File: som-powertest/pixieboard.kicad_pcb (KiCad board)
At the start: 8 copper layers, 50 x 50 mm, 138 parts, among them J1 Conn_02x20_Counter_Clockwise, J2 Conn_02x20_Counter_Clockwise, J3 Conn_02x20_Counter_Clockwise, J4 Conn_02x20_Counter_Clockwise, J5 Conn_02x20_Counter_Clockwise, J6 Conn_02x20_Counter_Clockwise, J7 Conn_02x20_Counter_Clockwise, U10 RS3236-ADJ8YF5, U5 SIC402, U6 RS3236-ADJ8YF5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

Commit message: Migrate evey power wire off layers in3-in6
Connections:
- J1 pad 10: Net-(J1-Pin_10) -> unconnected-(J1-Pin_10-Pad10)
- J1 pad 12: Net-(J1-Pin_12) -> unconnected-(J1-Pin_12-Pad12)
- J1 pad 13: Net-(J1-Pin_13) -> unconnected-(J1-Pin_13-Pad13)
- J1 pad 15: Net-(J1-Pin_15) -> unconnected-(J1-Pin_15-Pad15)
- J1 pad 16: Net-(J1-Pin_16) -> unconnected-(J1-Pin_16-Pad16)
- J1 pad 18: Net-(J1-Pin_18) -> unconnected-(J1-Pin_18-Pad18)
- J1 pad 19: Net-(J1-Pin_19) -> unconnected-(J1-Pin_19-Pad19)
- J1 pad 22: Net-(J1-Pin_19) -> unconnected-(J1-Pin_22-Pad22)
- J1 pad 23: Net-(J1-Pin_18) -> unconnected-(J1-Pin_23-Pad23)
- J1 pad 25: Net-(J1-Pin_16) -> unconnected-(J1-Pin_25-Pad25)
- J1 pad 26: Net-(J1-Pin_15) -> unconnected-(J1-Pin_26-Pad26)
- J1 pad 28: Net-(J1-Pin_13) -> unconnected-(J1-Pin_28-Pad28)
- J1 pad 29: Net-(J1-Pin_12) -> unconnected-(J1-Pin_29-Pad29)
- J1 pad 31: Net-(J1-Pin_10) -> unconnected-(J1-Pin_31-Pad31)
- J1 pad 32: Net-(J1-Pin_32) -> unconnected-(J1-Pin_32-Pad32)
- J1 pad 9: Net-(J1-Pin_32) -> unconnected-(J1-Pin_9-Pad9)
- J2 pad 11: Net-(J2-Pin_11) -> unconnected-(J2-Pin_11-Pad11)
- J2 pad 12: Net-(J2-Pin_12) -> unconnected-(J2-Pin_12-Pad12)
- J2 pad 14: Net-(J2-Pin_14) -> unconnected-(J2-Pin_14-Pad14)
- J2 pad 15: Net-(J2-Pin_15) -> unconnected-(J2-Pin_15-Pad15)
- J2 pad 17: Net-(J2-Pin_17) -> unconnected-(J2-Pin_17-Pad17)
- J2 pad 18: Net-(J2-Pin_18) -> unconnected-(J2-Pin_18-Pad18)
- J2 pad 2: Net-(J2-Pin_2) -> unconnected-(J2-Pin_2-Pad2)
- J2 pad 23: Net-(J2-Pin_18) -> unconnected-(J2-Pin_23-Pad23)
- J2 pad 24: Net-(J2-Pin_17) -> unconnected-(J2-Pin_24-Pad24)
- J2 pad 26: Net-(J2-Pin_15) -> unconnected-(J2-Pin_26-Pad26)
- J2 pad 27: Net-(J2-Pin_14) -> unconnected-(J2-Pin_27-Pad27)
- J2 pad 29: Net-(J2-Pin_12) -> unconnected-(J2-Pin_29-Pad29)
- J2 pad 3: Net-(J2-Pin_3) -> unconnected-(J2-Pin_3-Pad3)
- J2 pad 30: Net-(J2-Pin_11) -> unconnected-(J2-Pin_30-Pad30)
- J2 pad 32: Net-(J2-Pin_32) -> unconnected-(J2-Pin_32-Pad32)
- J2 pad 33: Net-(J2-Pin_33) -> unconnected-(J2-Pin_33-Pad33)
- J2 pad 35: Net-(J2-Pin_35) -> unconnected-(J2-Pin_35-Pad35)
- J2 pad 36: Net-(J2-Pin_36) -> unconnected-(J2-Pin_36-Pad36)
- J2 pad 38: Net-(J2-Pin_3) -> unconnected-(J2-Pin_38-Pad38)
- J2 pad 39: Net-(J2-Pin_2) -> unconnected-(J2-Pin_39-Pad39)
- J2 pad 5: Net-(J2-Pin_36) -> unconnected-(J2-Pin_5-Pad5)
- J2 pad 6: Net-(J2-Pin_35) -> unconnected-(J2-Pin_6-Pad6)
- J2 pad 8: Net-(J2-Pin_33) -> unconnected-(J2-Pin_8-Pad8)
- J2 pad 9: Net-(J2-Pin_32) -> unconnected-(J2-Pin_9-Pad9)
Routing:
- net /DDR_VREF: track 88.5 -> 75.2 mm, vias 8 -> 0
- net /DDR3/V_{TT}: track 70.8 -> 66.5 mm, vias 7 -> 2
- net MTGAVTT: track 38.0 -> 34.7 mm, vias 7 -> 3
- net GND: track 80.0 -> 78.3 mm
- net MTGAVCC: vias 6 -> 1
- net +1V35: vias 49 -> 15
- added copper zone on In2.Cu, net +1V35
- added copper zone on In1.Cu, net /DDR3/V_{TT}
- removed copper zone on In3.Cu, net +1V35
- removed copper zone on In5.Cu, net /DDR3/V_{TT}

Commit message: Remove layers in3-in6 from powertest pcb
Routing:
- net MTGAVTT: vias 3 -> 1
- added copper zone on In2.Cu, net GND
- removed copper zone on In5.Cu, net +1V0
- removed copper zone on In3.Cu, net GND
- removed copper zone on In5.Cu, net GND
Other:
- copper layers 8 -> 4
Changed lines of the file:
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@@
 		(4 "In1.Cu" power)
 		(6 "In2.Cu" signal)
-		(8 "In3.Cu" power)
-		(10 "In4.Cu" signal)
-		(12 "In5.Cu" power)
-		(14 "In6.Cu" signal)
 		(2 "B.Cu" power)
 		(13 "F.Paste" user)
@@
 			(layer "dielectric 1"
 				(type "prepreg")
-				(thickness 0.0994)
+				(thickness 0.1)
 				(material "FR4")
 				(epsilon_r 4.5)
@@
 			(layer "dielectric 2"
 				(type "core")
-				(thickness 0.2)
+				(thickness 0.8772)
 				(material "FR4")
 				(epsilon_r 4.5)
@@
 			(layer "dielectric 3"
 				(type "prepreg")
-				(thickness 0.1088)
-				(material "FR4")
-				(epsilon_r 4.5)
-				(loss_tangent 0.02)
-			)
-			(layer "In3.Cu"
-				(type "copper")
-				(thickness 0.0152)
-			)
-			(layer "dielectric 4"
-				(type "core")
-				(thickness 0.2)
-				(material "FR4")
-				(epsilon_r 4.5)
-				(loss_tangent 0.02)
-			)
-			(layer "In4.Cu"
-				(type "copper")
-				(thickness 0.0152)
-			)
-			(layer "dielectric 5"
-				(type "prepreg")
-				(thickness 0.1088)
-				(material "FR4")
-				(epsilon_r 4.5)
-				(loss_tangent 0.02)
-			)
-			(layer "In5.Cu"
-				(type "copper")
-				(thickness 0.0152)
-			)
-			(layer "dielectric 6"
-				(type "core")
-				(thickness 0.2)
-				(material "FR4")
-				(epsilon_r 4.5)
-				(loss_tangent 0.02)
-			)
-			(layer "In6.Cu"
-				(type "copper")
-				(thickness 0.0152)
-			)
-			(layer "dielectric 7"
-				(type "prepreg")
-				(thickness 0.0994)
+				(thickness 0.1)
 				(material "FR4")
 				(epsilon_r 4.5)
@@
 		(net 41)
 	)
-	(via
-		(at 97.5 91.5)
-		(size 0.3)
-		(drill 0.15)
-		(layers "F.Cu" "B.Cu")
-		(net 41)
-	)
-	(via
-		(at 98.5 90.500001)
-		(size 0.3)
-		(drill 0.15)
-		(layers "F.Cu" "B.Cu")
-		(net 41)
-	)
 	(segment
 		(start 100.5 90.5)
@@
 	)
 	(segment
-		(start 97.5 91.5)
-		(end 97.500001 91.5)
-		(width 0.15)
-		(layer "In6.Cu")
-		(net 41)
-	)
-	(segment
-		(start 98.5 90.500001)
-		(end 98.500001 90.500001)
-		(width 0.15)
-		(layer "In6.Cu")
-		(net 41)
-	)
-	(segment
 		(start 112.75 86.45)
 		(end 112.8975 86.5975)
@@
 		(polygon
 			(pts
-				(xy 77.1 95.4) (xy 80.7 95.4) (xy 80.7 95.8) (xy 77.1 95.8)
-			)
-		)
-	)
-	(zone
-		(net 0)
-		(net_name "")
-		(layer "B.Cu")
-		(hatch edge 0.5)
-		(connect_pads
-			(clearance 0)
-		)
-		(min_thickness 0.25)
-		(filled_areas_thickness no)
-		(keepout
-			(tracks allowed)
-			(vias allowed)
-			(pads allowed)
-			(copperpour not_allowed)
-			(footprints allowed)
-		)
-		(placement
-			(enabled no)
-			(sheetname "")
-		)
-		(fill
-			(thermal_gap 0.5)
-			(thermal_bridge_width 0.5)
-		)
-		(polygon
-			(pts
 				(xy 109.2 78.4) (xy 114.4 78.4) (xy 114.4 78.8) (xy 109.2 78.8)
 			)
@@
 		(polygon
 			(pts
-				(xy 77.1 89.4) (xy 77.1 89) (xy 80.7 89) (xy 80.7 89.4)
-			)
-		)
-	)
-	(zone
-		(net 0)
-		(net_name "")
-		(layer "B.Cu")
-		(hatch edge 0.5)
-		(connect_pads
-			(clearance 0)
-		)
-		(min_thickness 0.25)
-		(filled_areas_thickness no)
-		(keepout
-			(tracks allowed)
-			(vias allowed)
-			(pads allowed)
-			(copperpour not_allowed)
-			(footprints allowed)
-		)
-		(placement
-			(enabled no)
-			(sheetname "")
-		)
-		(fill
-			(thermal_gap 0.5)
-			(thermal_bridge_width 0.5)
-		)
-		(polygon
-			(pts
 				(xy 82.5 117.8) (xy 84.7 117.8) (xy 84.7 118.2) (xy 82.5 118.2)
 			)
@@
 		(net 3)
 		(net_name "GND")
-		(layers "B.Cu" "In1.Cu" "In3.Cu" "In5.Cu")
+		(layers "B.Cu" "In1.Cu" "In2.Cu")
 		(hatch edge 0.5)
 		(connect_pads
@@
 		(net 7)
 		(net_name "+1V0")
-		(layers "In1.Cu" "In5.Cu")
+		(layer "In1.Cu")
 		(hatch edge 0.5)
 		(priority 2)

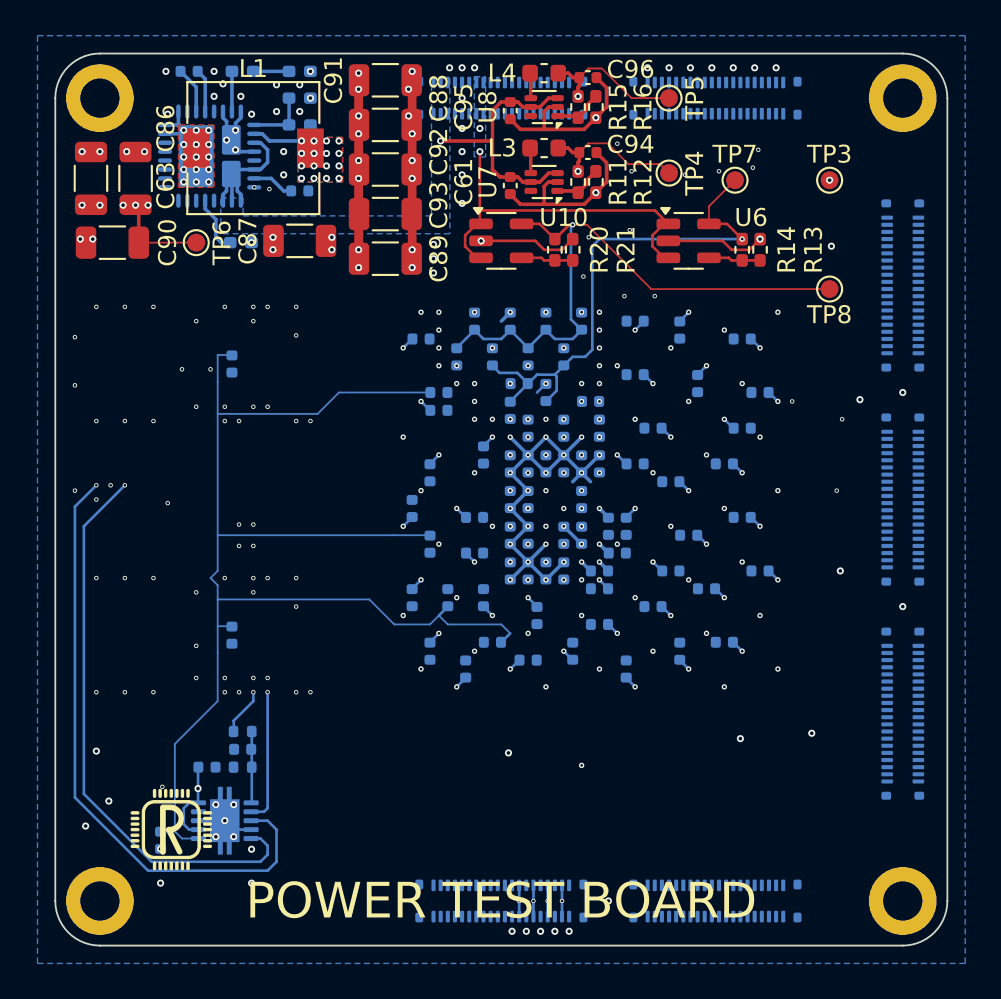
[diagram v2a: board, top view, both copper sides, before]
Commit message: Add large pads for connection to a synthetic load
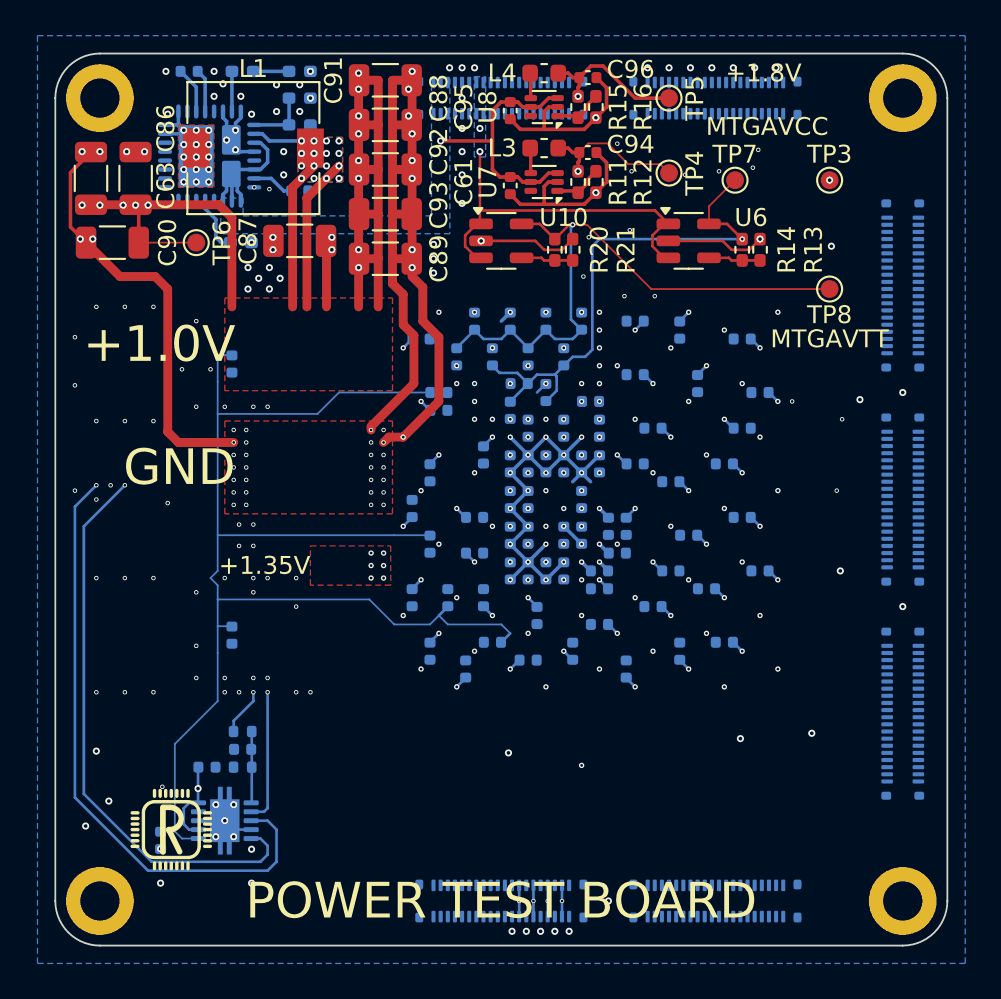
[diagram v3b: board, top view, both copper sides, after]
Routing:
- net GND: track 78.3 -> 140.5 mm, vias 248 -> 268
- net +1V0: track 19.2 -> 74.0 mm
- net +1V35: vias 15 -> 21
- added copper zone on F.Cu, net +1V35
- added copper zone on F.Cu, net GND
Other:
- board text added: "+1.0V"
- board text added: "+1.35V"
- board text added: "+1.8V"
- board text added: "GND"
- board text added: "MTGAVCC"
- board text added: "MTGAVTT"
